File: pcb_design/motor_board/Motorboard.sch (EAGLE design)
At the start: 78 parts, among them M1 STEPPER_MOTOR_SMD, M2 STEPPER_MOTOR_SMD

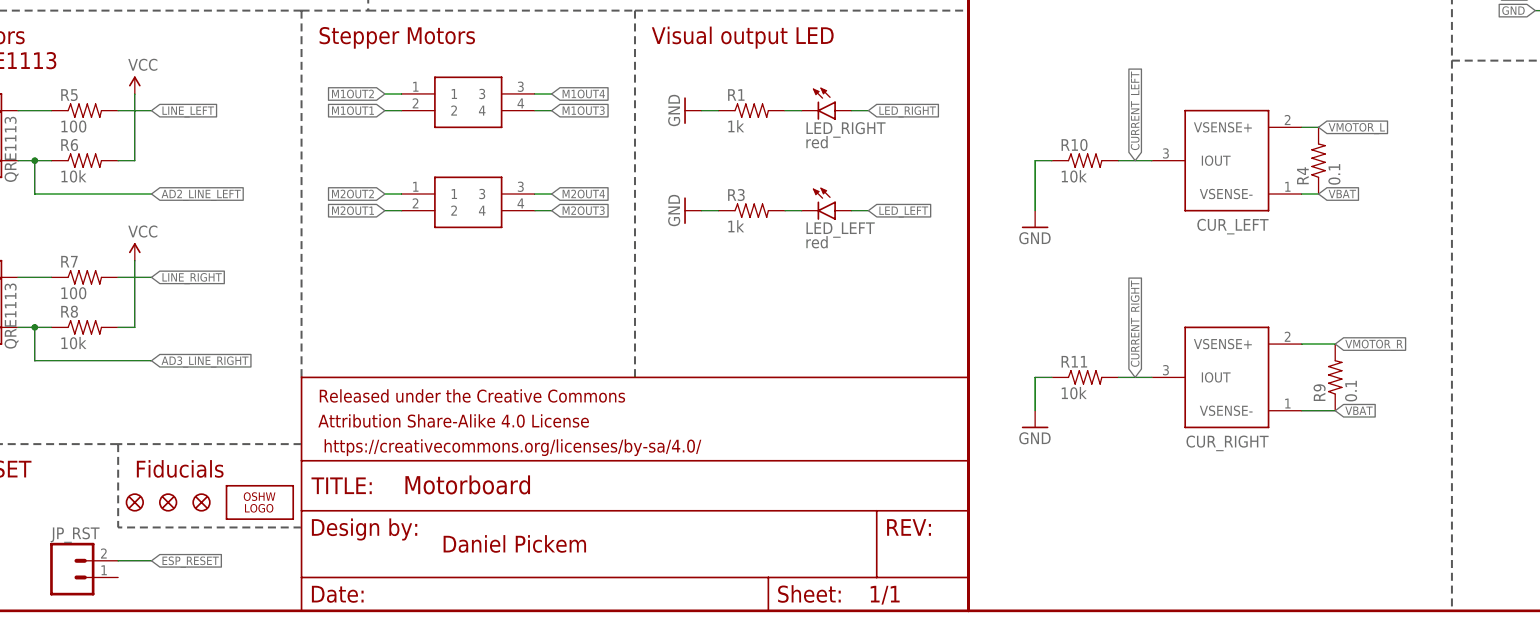
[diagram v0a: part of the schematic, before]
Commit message: Updated the GRITSBot's motor board
1. Added a reset pin so that the main board can reset
    the motor board.
2. Fixed the polarity of the current sensors.
3. Added test pins on the top layer.
4. Added castellated edges to mount motors mechanically
    more stable.
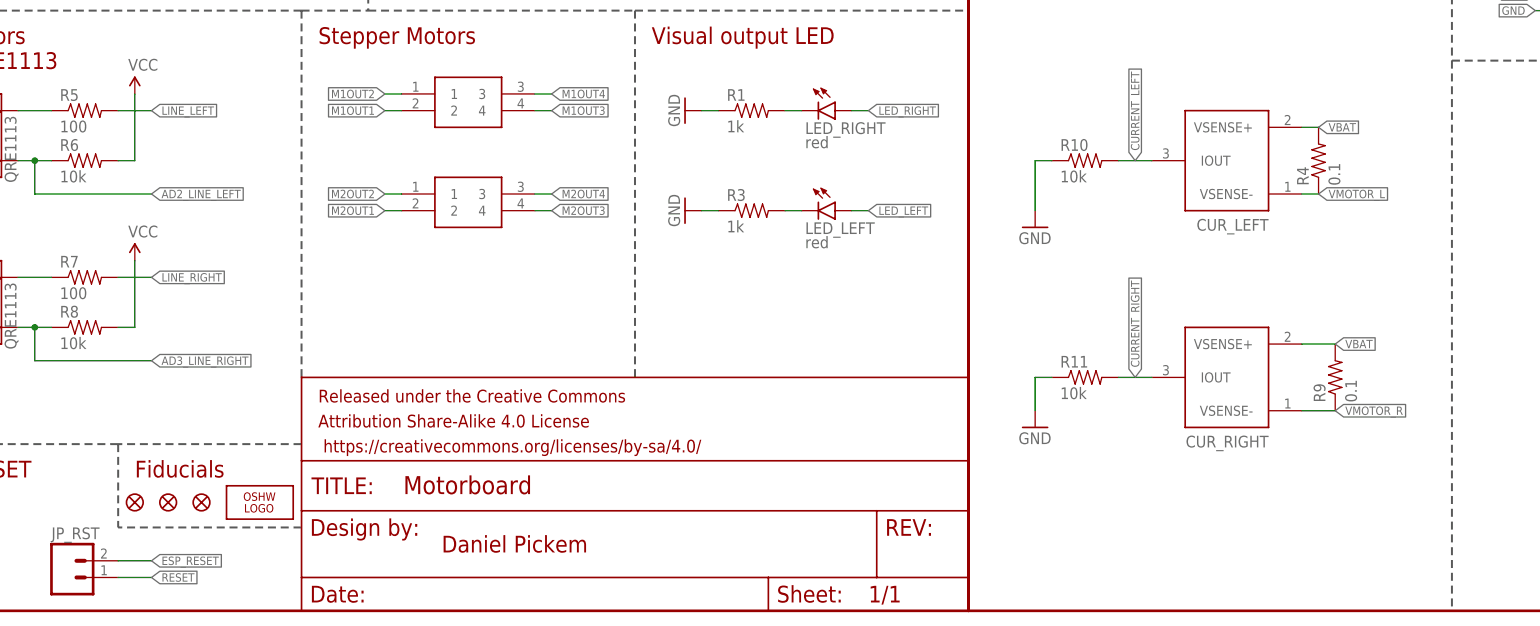
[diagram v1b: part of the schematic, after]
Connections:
- net RESET: now also JP_RST.1
- net VBAT: now also CUR_LEFT.VSENSE+, CUR_RIGHT.VSENSE+, R4.2, R9.2; no longer CUR_LEFT.VSENSE-, CUR_RIGHT.VSENSE-, R4.1, R9.1
- net VMOTOR_L: now also CUR_LEFT.VSENSE-, R4.1; no longer CUR_LEFT.VSENSE+, R4.2
- net VMOTOR_R: now also CUR_RIGHT.VSENSE-, R9.1; no longer CUR_RIGHT.VSENSE+, R9.2
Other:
- note added: "10102016: Added castellated edges for more stable motor mounting"
- note added: "19102016: Connected RST to breakout pin (so that main board can reset motor board)"
- note added: "19102016: Fixed polarity of current sensors"
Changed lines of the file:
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@@
 <?xml version="1.0" encoding="utf-8"?>
 <!DOCTYPE eagle SYSTEM "eagle.dtd">
-<eagle version="7.3.0">
+<eagle version="7.7.0">
 <drawing>
 <settings>
@@
 <text x="363.22" y="93.98" size="1.778" layer="98">TP6</text>
 <text x="363.22" y="91.44" size="1.778" layer="98">TP4</text>
+<text x="396.24" y="152.4" size="1.27" layer="98" align="top-left">10102016: Added castellated edges for more stable motor mounting</text>
+<text x="396.24" y="149.86" size="1.27" layer="98" align="top-left">19102016: Connected RST to breakout pin (so that main board can reset motor board)</text>
+<text x="396.24" y="147.32" size="1.27" layer="98" align="top-left">19102016: Fixed polarity of current sensors</text>
 </plain>
 <instances>
@@
 <pinref part="TP5" gate="G$1" pin="TP"/>
 </segment>
+<segment>
+<pinref part="JP_RST" gate="G$1" pin="1"/>
+<wire x1="119.38" y1="5.08" x2="124.46" y2="5.08" width="0.1524" layer="91"/>
+<label x="124.46" y="5.08" size="1.27" layer="95" xref="yes"/>
+</segment>
 </net>
 <net name="N$2" class="0">
@@
 </segment>
 <segment>
-<pinref part="CUR_RIGHT" gate="G$1" pin="VSENSE-"/>
-<pinref part="R9" gate="G$1" pin="1"/>
-<wire x1="299.72" y1="30.48" x2="304.8" y2="30.48" width="0.1524" layer="91"/>
-<label x="304.8" y="30.48" size="1.27" layer="95" xref="yes"/>
-</segment>
-<segment>
-<pinref part="CUR_LEFT" gate="G$1" pin="VSENSE-"/>
-<pinref part="R4" gate="G$1" pin="1"/>
-<wire x1="299.72" y1="63.5" x2="302.26" y2="63.5" width="0.1524" layer="91"/>
-<label x="302.26" y="63.5" size="1.27" layer="95" xref="yes"/>
+<pinref part="CUR_LEFT" gate="G$1" pin="VSENSE+"/>
+<pinref part="R4" gate="G$1" pin="2"/>
+<wire x1="299.72" y1="73.66" x2="302.26" y2="73.66" width="0.1524" layer="91"/>
+<label x="302.26" y="73.66" size="1.27" layer="95" xref="yes"/>
+</segment>
+<segment>
+<pinref part="CUR_RIGHT" gate="G$1" pin="VSENSE+"/>
+<pinref part="R9" gate="G$1" pin="2"/>
+<wire x1="299.72" y1="40.64" x2="304.8" y2="40.64" width="0.1524" layer="91"/>
+<label x="304.8" y="40.64" size="1.27" layer="95" xref="yes"/>
 </segment>
 </net>
@@
 </segment>
 <segment>
-<pinref part="CUR_LEFT" gate="G$1" pin="VSENSE+"/>
-<pinref part="R4" gate="G$1" pin="2"/>
-<wire x1="299.72" y1="73.66" x2="302.26" y2="73.66" width="0.1524" layer="91"/>
-<label x="302.26" y="73.66" size="1.27" layer="95" xref="yes"/>
-</segment>
-<segment>
 <pinref part="MOTOR_CTRL_L" gate="G$1" pin="VS2"/>
 <wire x1="226.06" y1="162.56" x2="228.6" y2="162.56" width="0.1524" layer="91"/>
 <label x="228.6" y="162.56" size="1.27" layer="95" xref="yes"/>
+</segment>
+<segment>
+<pinref part="CUR_LEFT" gate="G$1" pin="VSENSE-"/>
+<pinref part="R4" gate="G$1" pin="1"/>
+<wire x1="299.72" y1="63.5" x2="302.26" y2="63.5" width="0.1524" layer="91"/>
+<label x="302.26" y="63.5" size="1.27" layer="95" xref="yes"/>
 </segment>
 </net>
@@
 </segment>
 <segment>
-<pinref part="CUR_RIGHT" gate="G$1" pin="VSENSE+"/>
-<pinref part="R9" gate="G$1" pin="2"/>
-<wire x1="299.72" y1="40.64" x2="304.8" y2="40.64" width="0.1524" layer="91"/>
-<label x="304.8" y="40.64" size="1.27" layer="95" xref="yes"/>
-</segment>
-<segment>
 <pinref part="MOTOR_CTRL_R" gate="G$1" pin="VS2"/>
 <wire x1="226.06" y1="127" x2="228.6" y2="127" width="0.1524" layer="91"/>
 <label x="228.6" y="127" size="1.27" layer="95" xref="yes"/>
 </segment>
-</net>
+<segment>
+<pinref part="CUR_RIGHT" gate="G$1" pin="VSENSE-"/>
+<pinref part="R9" gate="G$1" pin="1"/>
+<wire x1="299.72" y1="30.48" x2="304.8" y2="30.48" width="0.1524" layer="91"/>
+<label x="304.8" y="30.48" size="1.27" layer="95" xref="yes"/>
+</segment>
+</net>

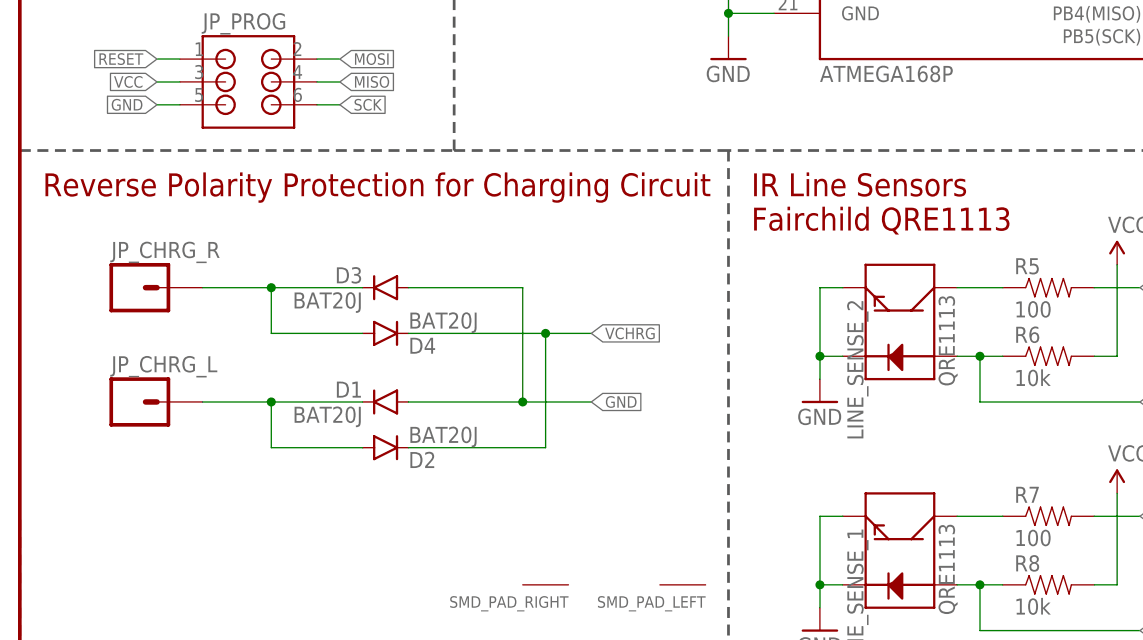
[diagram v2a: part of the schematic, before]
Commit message: Removed reverse polarity protection on charge input
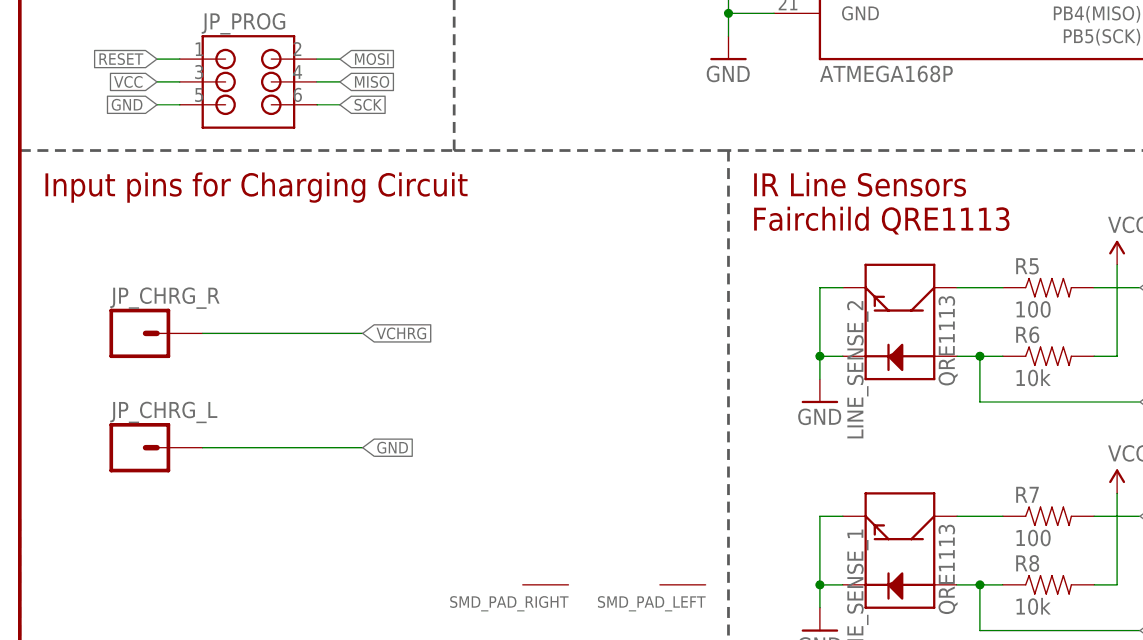
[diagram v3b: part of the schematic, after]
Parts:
- removed D1, D2, D3, D4: BAT20J, SparkFun-DiscreteSemi:DIODEBAS16
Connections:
- removed net PAD_LEFT: D1.C, D2.A, JP_CHRG_L.1
- removed net PAD_RIGHT: D3.C, D4.A, JP_CHRG_R.1
- net GND: now also JP_CHRG_L.1; no longer D1.A, D3.A
- net VCHRG: now also JP_CHRG_R.1; no longer D2.C, D4.C
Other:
- note added: "25102016: Removed reverse polarity protection diodes since they lower charge voltage too much"
- note added: "Input pins for Charging Circuit"
- note removed: "NOTE: BAT20J diodes have a low forward voltage drop of 0.28 - 0.54V depending on forward current."
- note removed: "Reverse Polarity Protection for Charging Circuit"
- moved on the sheet: JP_CHRG_L, JP_CHRG_R
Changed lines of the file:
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@@
 <part name="SMD_PAD_RIGHT" library="GRITSBot" deviceset="PIN_SMD" device="2.5X1.0"/>
 <part name="FRAME1" library="GRITSBot" deviceset="FRAME-LETTER" device=""/>
-<part name="D1" library="SparkFun-DiscreteSemi" deviceset="DIODE" device="BAS16" value="BAT20J"/>
-<part name="D2" library="SparkFun-DiscreteSemi" deviceset="DIODE" device="BAS16" value="BAT20J"/>
-<part name="D3" library="SparkFun-DiscreteSemi" deviceset="DIODE" device="BAS16" value="BAT20J"/>
-<part name="D4" library="SparkFun-DiscreteSemi" deviceset="DIODE" device="BAS16" value="BAT20J"/>
 <part name="SMD_PAD_LEFT" library="GRITSBot" deviceset="PIN_SMD" device="2.5X1.0"/>
 <part name="JP_VCHRG" library="SparkFun-Connectors" deviceset="M02" device="1X02_NO_SILK"/>
@@
 <text x="50.8" y="45.72" size="1.778" layer="98">SMD pads for soldering
 on motor brackets</text>
-<text x="2.54" y="86.36" size="2.54" layer="94">Reverse Polarity Protection for Charging Circuit</text>
+<text x="2.54" y="86.36" size="2.54" layer="94">Input pins for Charging Circuit</text>
 <text x="396.24" y="182.88" size="1.778" layer="98" align="top-left">Changelog:
 </text>
@@
 (pull-up resistors
 on main board)</text>
-<text x="2.54" y="38.1" size="1.778" layer="98">NOTE: BAT20J diodes have
-           a low forward voltage
-           drop of 0.28 - 0.54V
-           depending on forward
-           current.</text>
 <text x="38.354" y="112.522" size="1.778" layer="98" rot="R180">Programming header
 for Atmega chip</text>
@@
             Atmega168 or 328 chip</text>
 <text x="81.28" y="27.94" size="1.778" layer="98">Downward-facing IR sensors for line-following applications</text>
-<text x="33.02" y="81.28" size="1.778" layer="98">NOTE: Max. charge input voltage is 6V.</text>
+<text x="33.02" y="76.2" size="1.778" layer="98">NOTE: Max. charge input voltage is 6V.</text>
 <text x="251.46" y="170.18" size="1.778" layer="98">NOTE: These sensors measure motor temperatures for
             maintenance and diagnostic purposes.</text>
@@
 <text x="396.24" y="149.86" size="1.27" layer="98" align="top-left">19102016: Connected RST to breakout pin (so that main board can reset motor board)</text>
 <text x="396.24" y="147.32" size="1.27" layer="98" align="top-left">19102016: Fixed polarity of current sensors</text>
+<text x="396.24" y="144.78" size="1.27" layer="98" align="top-left">25102016: Removed reverse polarity protection diodes since they lower charge voltage too much</text>
 </plain>
 <instances>
@@
 <instance part="FRAME1" gate="G$1" x="0" y="0"/>
 <instance part="FRAME1" gate="G$2" x="147.32" y="0"/>
-<instance part="D1" gate="G$1" x="40.64" y="63.5" rot="MR0"/>
-<instance part="D2" gate="G$1" x="40.64" y="58.42" rot="MR180"/>
-<instance part="D3" gate="G$1" x="40.64" y="76.2" rot="MR0"/>
-<instance part="D4" gate="G$1" x="40.64" y="71.12" rot="MR180"/>
 <instance part="SMD_PAD_LEFT" gate="G$1" x="71.12" y="43.18" smashed="yes" rot="R180">
 <attribute name="NAME" x="76.2" y="41.91" size="1.27" layer="95" rot="R180"/>
@@
 </instance>
 <instance part="JP5" gate="G$1" x="132.08" y="16.51"/>
-<instance part="JP_CHRG_L" gate="G$1" x="12.7" y="63.5" smashed="yes">
-<attribute name="NAME" x="10.16" y="66.802" size="1.778" layer="95"/>
-</instance>
-<instance part="JP_CHRG_R" gate="G$1" x="12.7" y="76.2" smashed="yes">
-<attribute name="NAME" x="10.16" y="79.502" size="1.778" layer="95"/>
+<instance part="JP_CHRG_L" gate="G$1" x="12.7" y="58.42" smashed="yes">
+<attribute name="NAME" x="10.16" y="61.722" size="1.778" layer="95"/>
+</instance>
+<instance part="JP_CHRG_R" gate="G$1" x="12.7" y="71.12" smashed="yes">
+<attribute name="NAME" x="10.16" y="74.422" size="1.778" layer="95"/>
 </instance>
 <instance part="CUR_RIGHT" gate="G$1" x="289.56" y="35.56" smashed="yes" rot="R180">
@@
 </segment>
 <segment>
-<pinref part="D1" gate="G$1" pin="A"/>
-<wire x1="43.18" y1="63.5" x2="55.88" y2="63.5" width="0.1524" layer="91"/>
-<label x="63.5" y="63.5" size="1.27" layer="95" xref="yes"/>
-<pinref part="D3" gate="G$1" pin="A"/>
-<wire x1="55.88" y1="63.5" x2="63.5" y2="63.5" width="0.1524" layer="91"/>
-<wire x1="43.18" y1="76.2" x2="55.88" y2="76.2" width="0.1524" layer="91"/>
-<wire x1="55.88" y1="76.2" x2="55.88" y2="63.5" width="0.1524" layer="91"/>
-<junction x="55.88" y="63.5"/>
+<label x="38.1" y="58.42" size="1.27" layer="95" xref="yes"/>
+<pinref part="JP_CHRG_L" gate="G$1" pin="1"/>
+<wire x1="20.32" y1="58.42" x2="38.1" y2="58.42" width="0.1524" layer="91"/>
 </segment>
 <segment>
@@
 </segment>
 <segment>
-<pinref part="D4" gate="G$1" pin="C"/>
-<wire x1="43.18" y1="71.12" x2="58.42" y2="71.12" width="0.1524" layer="91"/>
-<label x="63.5" y="71.12" size="1.27" layer="95" xref="yes"/>
-<pinref part="D2" gate="G$1" pin="C"/>
-<wire x1="58.42" y1="71.12" x2="63.5" y2="71.12" width="0.1524" layer="91"/>
-<wire x1="43.18" y1="58.42" x2="58.42" y2="58.42" width="0.1524" layer="91"/>
-<wire x1="58.42" y1="58.42" x2="58.42" y2="71.12" width="0.1524" layer="91"/>
-<junction x="58.42" y="71.12"/>
+<label x="38.1" y="71.12" size="1.27" layer="95" xref="yes"/>
+<wire x1="20.32" y1="71.12" x2="38.1" y2="71.12" width="0.1524" layer="91"/>
+<pinref part="JP_CHRG_R" gate="G$1" pin="1"/>
 </segment>
 <segment>
@@
 </segment>
 </net>
-<net name="PAD_LEFT" class="0">
-<segment>
-<pinref part="JP_CHRG_L" gate="G$1" pin="1"/>
-<pinref part="D1" gate="G$1" pin="C"/>
-<wire x1="38.1" y1="63.5" x2="27.94" y2="63.5" width="0.1524" layer="91"/>
-<pinref part="D2" gate="G$1" pin="A"/>
-<wire x1="27.94" y1="63.5" x2="20.32" y2="63.5" width="0.1524" layer="91"/>
-<wire x1="38.1" y1="58.42" x2="27.94" y2="58.42" width="0.1524" layer="91"/>
-<wire x1="27.94" y1="58.42" x2="27.94" y2="63.5" width="0.1524" layer="91"/>
-<junction x="27.94" y="63.5"/>
-</segment>
-</net>
-<net name="PAD_RIGHT" class="0">
-<segment>
-<pinref part="JP_CHRG_R" gate="G$1" pin="1"/>
-<pinref part="D4" gate="G$1" pin="A"/>
-<wire x1="38.1" y1="71.12" x2="27.94" y2="71.12" width="0.1524" layer="91"/>
-<pinref part="D3" gate="G$1" pin="C"/>
-<wire x1="38.1" y1="76.2" x2="27.94" y2="76.2" width="0.1524" layer="91"/>
-<wire x1="27.94" y1="76.2" x2="27.94" y2="71.12" width="0.1524" layer="91"/>
-<wire x1="20.32" y1="76.2" x2="27.94" y2="76.2" width="0.1524" layer="91"/>
-<junction x="27.94" y="76.2"/>
-</segment>
-</net>

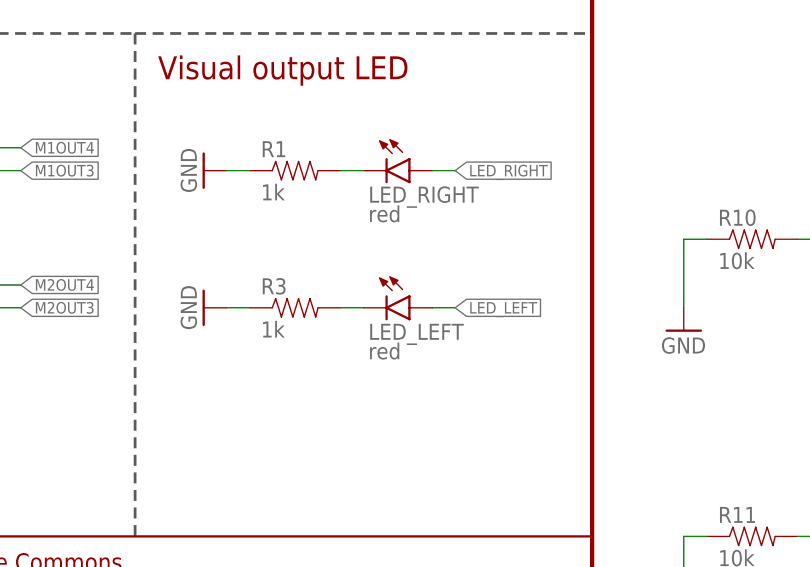
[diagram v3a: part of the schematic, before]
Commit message: Changed LED color value on motor board
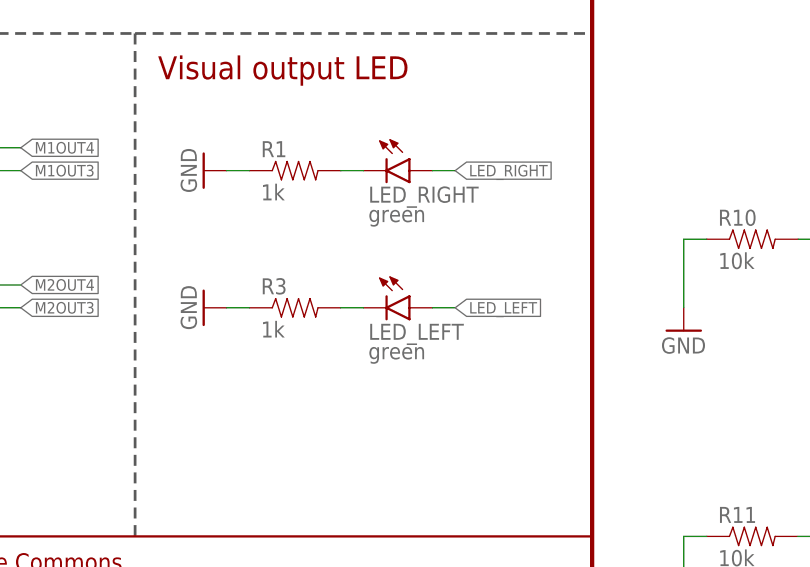
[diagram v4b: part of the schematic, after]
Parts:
- LED_LEFT, LED_RIGHT: value red -> green
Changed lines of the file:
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@@
 <part name="R8" library="SparkFun-Resistors" deviceset="1.5KOHM1/10W1%(0603)" device="" value="10k"/>
 <part name="ATMEGA168P" library="GRITSBot" deviceset="ATMEGA168" device=""/>
-<part name="LED_RIGHT" library="SparkFun-LED" deviceset="LED" device="0603" value="red"/>
+<part name="LED_RIGHT" library="SparkFun-LED" deviceset="LED" device="0603" value="green"/>
 <part name="R1" library="SparkFun-Resistors" deviceset="1.5KOHM1/10W1%(0603)" device="" value="1k"/>
 <part name="GND1" library="SparkFun-Aesthetics" deviceset="GND" device=""/>
@@
 <part name="JP_GND" library="SparkFun-Connectors" deviceset="M02" device="1X02_NO_SILK"/>
 <part name="JP_PROG" library="GRITSBot" deviceset="3X2_SMD_HEADER" device=""/>
-<part name="LED_LEFT" library="SparkFun-LED" deviceset="LED" device="0603" value="red"/>
+<part name="LED_LEFT" library="SparkFun-LED" deviceset="LED" device="0603" value="green"/>
 <part name="R3" library="SparkFun-Resistors" deviceset="1.5KOHM1/10W1%(0603)" device="" value="1k"/>
 <part name="GND2" library="SparkFun-Aesthetics" deviceset="GND" device=""/>
